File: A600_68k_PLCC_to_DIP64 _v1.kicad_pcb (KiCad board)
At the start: 4 copper layers, 101.6 x 102.9 mm, 17 parts, among them J1 171826-4, U1 MC68000_PLCC68, U2 68000_SOCKET

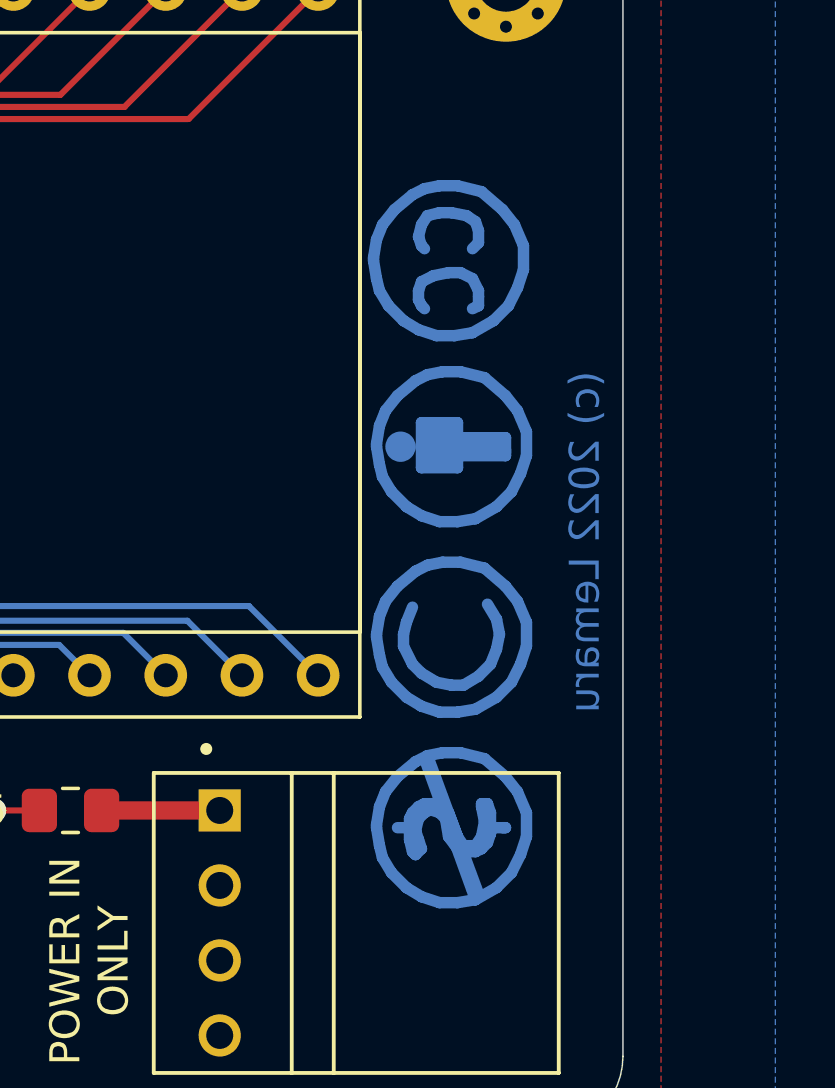
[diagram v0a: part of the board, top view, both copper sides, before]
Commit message: Corrected cap values
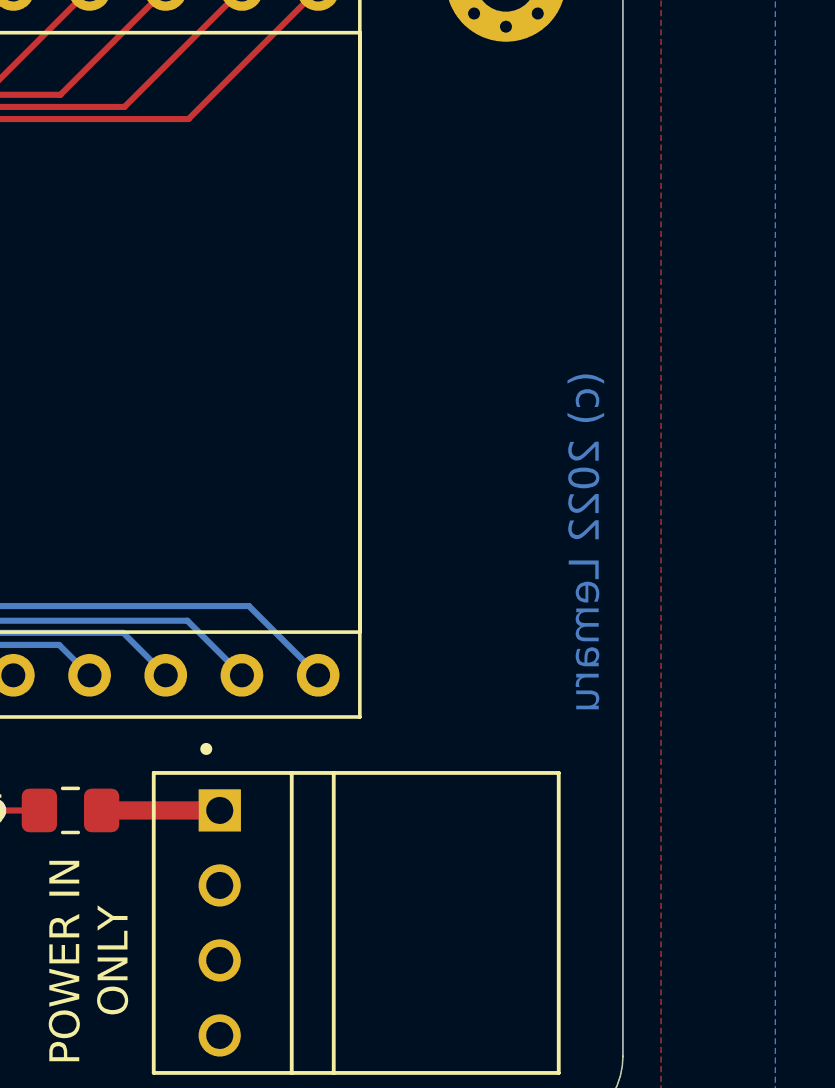
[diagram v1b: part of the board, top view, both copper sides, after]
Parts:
- removed REF**: Symbol_CC-Noncommercial_CopperTop_Small, Symbol:Symbol_CC-Noncommercial_CopperTop_Small
- removed REF**: Symbol_CC-ShareAlike_CopperTop_Small, Symbol:Symbol_CC-ShareAlike_CopperTop_Small
- removed REF**: Symbol_CC-Attribution_CopperTop_Small, Symbol:Symbol_CC-Attribution_CopperTop_Small
- removed REF**: Symbol_CreativeCommons_CopperTop_Type2_Small, Symbol:Symbol_CreativeCommons_CopperTop_Type2_Small
- C1, C2, C3, C4, C5: value 100nf -> 10uf
